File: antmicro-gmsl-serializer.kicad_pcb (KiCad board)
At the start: 4 copper layers, 43 x 43 mm, 95 parts, among them J1 Conn_FFC_WE_68715014022, J2 Conn_FAKRA_2FAI-NZSP-PCBB6, U1 AP62301_TSOT, U2 AP62301_TSOT, U3 NCP163ASN330T1G, U4 REF3012AIDBZT, U5 TLV73312PDBVT, U6 MAX9295A, Y1 Resonator_25MHz_ABM8G

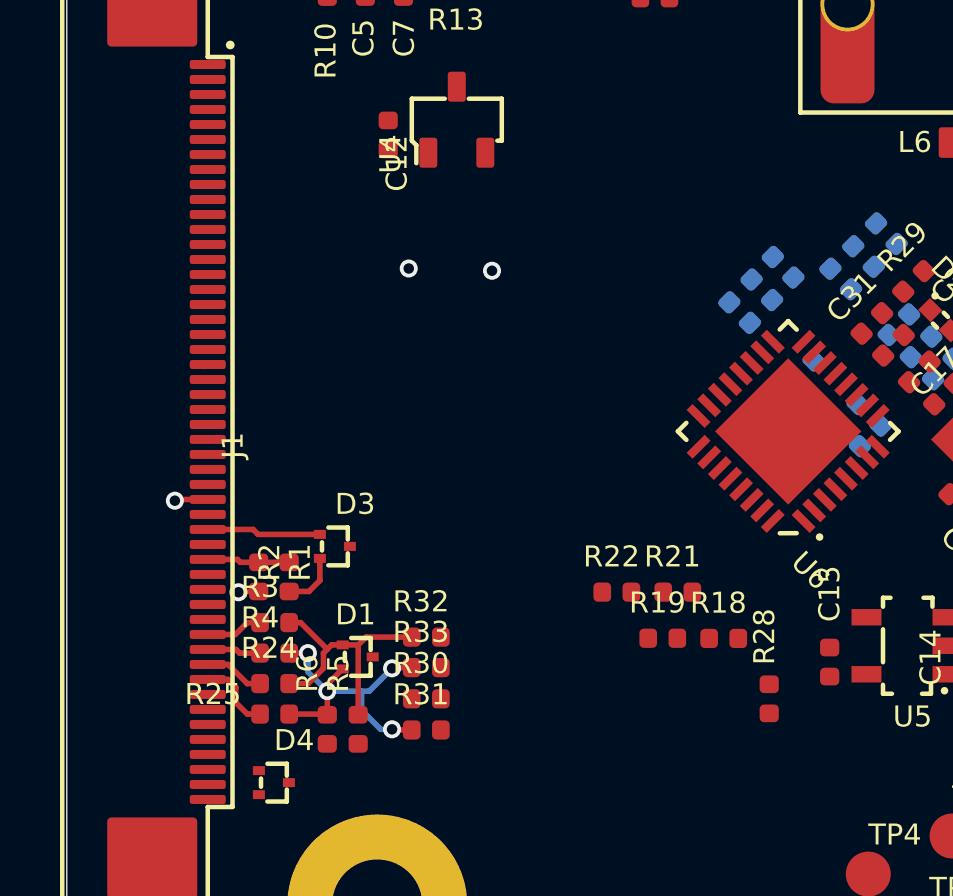
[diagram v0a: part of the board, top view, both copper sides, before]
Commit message: Route CSI lines
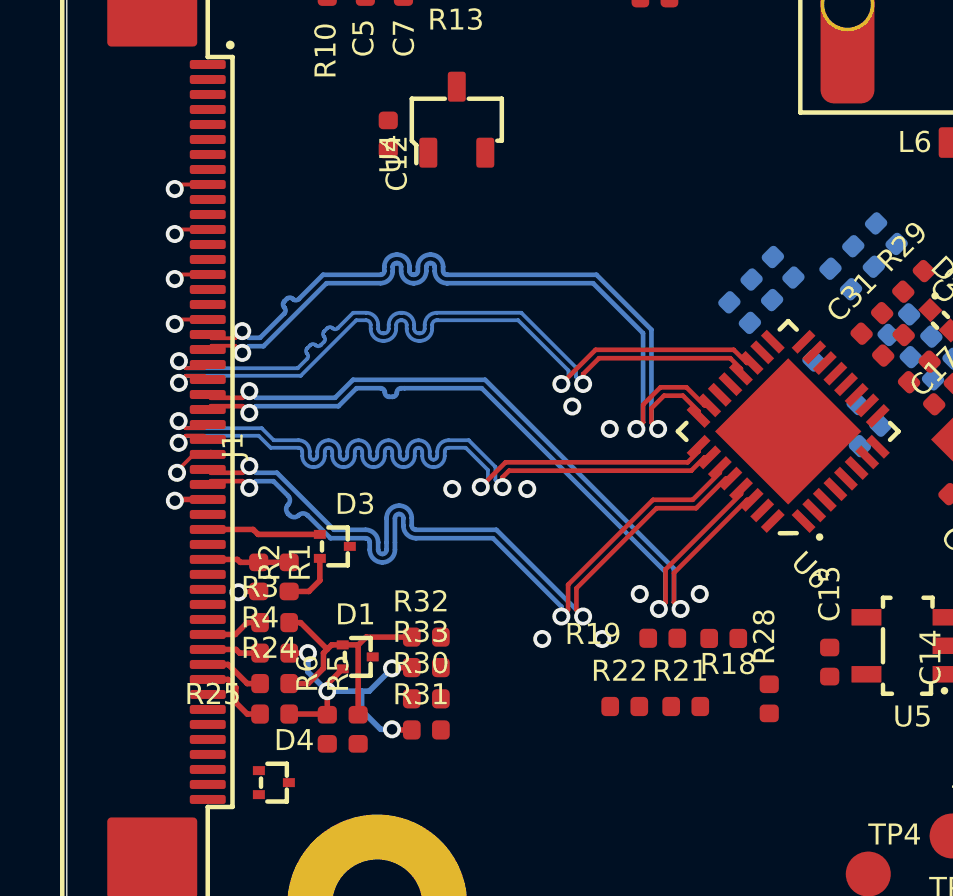
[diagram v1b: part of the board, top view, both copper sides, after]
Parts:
- moved R21 3.82 mm to (144.3, 111.0)
- moved R22 3.82 mm to (142.2, 111.0)
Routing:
- net CSI_D3_P: track 0.00 -> 25.4 mm, vias 0 -> 2
- net CSI_D2_P: track 0.07 -> 25.4 mm, vias 0 -> 2
- net CSI_D1_P: track 0.00 -> 25.2 mm, vias 0 -> 2
- net CSI_D0_P: track 0.00 -> 25.2 mm, vias 0 -> 2
- net CSI_D1_N: track 0.00 -> 25.2 mm, vias 0 -> 2
- net CSI_D3_N: track 0.00 -> 25.0 mm, vias 0 -> 2
- net CSI_CLK_P: track 0.00 -> 24.9 mm, vias 0 -> 2
- net CSI_CLK_N: track 0.00 -> 24.8 mm, vias 0 -> 2
- net CSI_D2_N: track 0.16 -> 25.0 mm, vias 0 -> 2
- net CSI_D0_N: track 0.00 -> 24.7 mm, vias 0 -> 2
- net GND: track 1.80 -> 7.90 mm, vias 4 -> 15

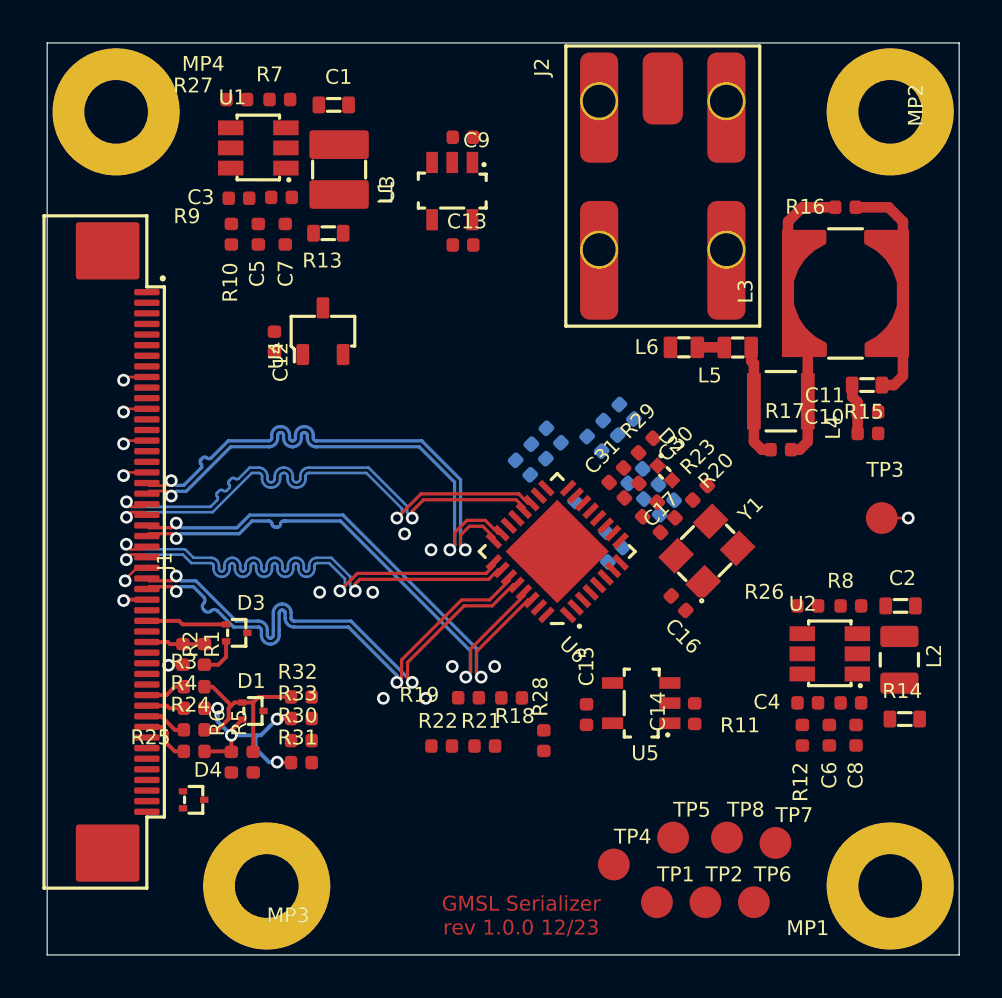
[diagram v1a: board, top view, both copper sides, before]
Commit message: Route I2C
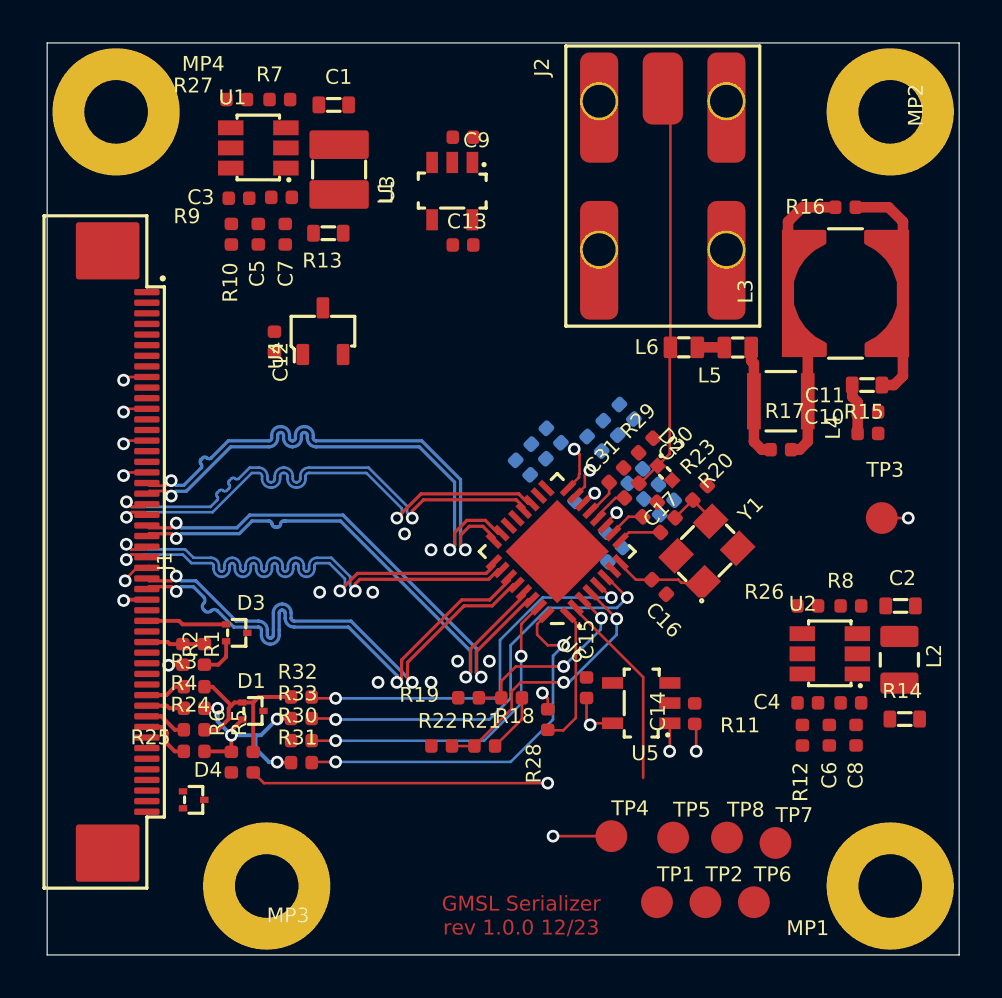
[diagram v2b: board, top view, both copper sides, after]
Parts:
- moved TP4 1.34 mm to (150.2, 115.2)
- moved C15 1.27 mm to (149.1, 108.2)
- moved C16 1.19 mm to (152.5, 103.5)
- moved R28 1.01 mm to (147.2, 109.8), turned to 90 degrees
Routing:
- net Net-(R33-Pad2): track 0.00 -> 20.2 mm, vias 0 -> 2
- net +3V3: track 0.00 -> 19.9 mm, vias 0 -> 4
- net SIO_P: track 0.00 -> 19.4 mm
- net Net-(R31-Pad2): track 0.00 -> 18.5 mm, vias 0 -> 2
- net Net-(R32-Pad2): track 0.00 -> 18.5 mm, vias 0 -> 2
- net Net-(R30-Pad2): track 0.00 -> 15.5 mm, vias 0 -> 2
- net /Serializer/CFG1: track 0.00 -> 12.9 mm, vias 0 -> 2
- net Net-(TP6-Pad1): track 0.00 -> 9.36 mm
- net /Serializer/CFG0: track 0.00 -> 9.31 mm, vias 0 -> 2
- net Net-(R28-Pad1): track 0.00 -> 6.76 mm
- net /Serializer/X1: track 0.00 -> 4.35 mm
- net +1V2: track 0.00 -> 3.90 mm, vias 0 -> 2
- net +1V8: track 0.00 -> 3.48 mm, vias 0 -> 3
- net /Serializer/VDDIO: track 0.00 -> 2.79 mm
- net /Serializer/X2_R: track 0.00 -> 2.54 mm
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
